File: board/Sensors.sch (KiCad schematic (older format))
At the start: 7 parts, among them Q1 Phototrans, Q2 Q_NPN_BEC, U1 74HC393

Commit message: Updated some refs.
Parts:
- C1: value 0.1uF/25V -> 0.1uF/50V
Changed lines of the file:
@@
 P 3800 3700
 F 0 "C1" H 3915 3746 50  0000 L CNN
-F 1 "0.1uF/25V" H 3915 3655 50  0000 L CNN
+F 1 "0.1uF/50V" H 3915 3655 50  0000 L CNN
 F 2 "Capacitor_SMD:C_0603_1608Metric_Pad1.05x0.95mm_HandSolder" H 3838 3550 50  0001 C CNN
 F 3 "~" H 3800 3700 50  0001 C CNN

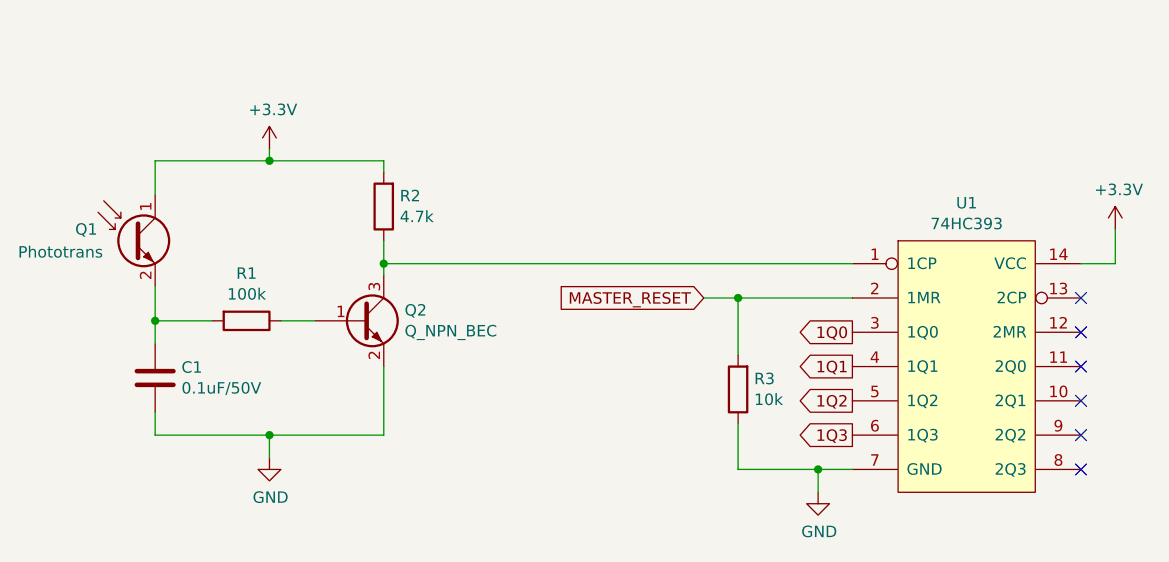
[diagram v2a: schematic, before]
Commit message: Reworked input circuit.
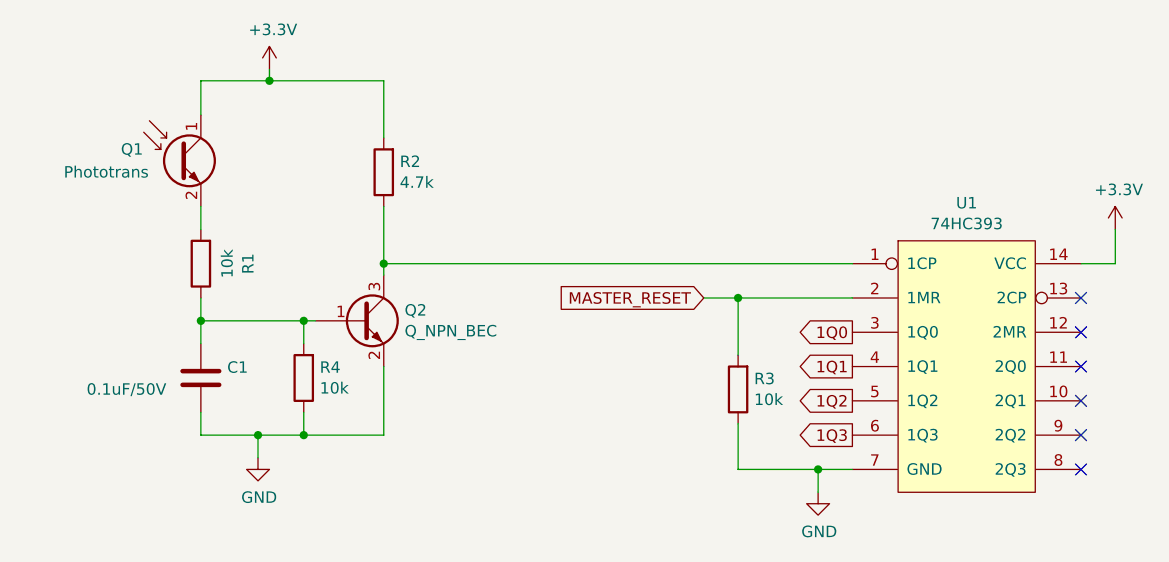
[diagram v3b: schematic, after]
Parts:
- added R4: 10k, Resistor_SMD:R_0603_1608Metric_Pad1.05x0.95mm_HandSolder, symbol Device:R
- R1: value 100k -> 10k
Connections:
- net GND: now also R4.1
- net at Q2.1 (B), R1.1: now also C1.1, R4.2
- net at Q1.2 (E), R1.2: no longer C1.1
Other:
- moved on the sheet: C1, Q1, R1, R2
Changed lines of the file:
@@
 L power:GND #PWR09
 U 1 1 5BE94315
-P 4300 4050
-F 0 "#PWR09" H 4300 3800 50  0001 C CNN
-F 1 "GND" H 4305 3877 50  0000 C CNN
-F 2 "" H 4300 4050 50  0001 C CNN
-F 3 "" H 4300 4050 50  0001 C CNN
-	1    4300 4050
+P 4250 4050
+F 0 "#PWR09" H 4250 3800 50  0001 C CNN
+F 1 "GND" H 4255 3877 50  0000 C CNN
+F 2 "" H 4250 4050 50  0001 C CNN
+F 3 "" H 4250 4050 50  0001 C CNN
+	1    4250 4050
 	1    0    0    -1
 $EndComp
@@
 L Device:C C1
 U 1 1 5BE943F3
-P 3800 3700
-F 0 "C1" H 3915 3746 50  0000 L CNN
-F 1 "0.1uF/50V" H 3915 3655 50  0000 L CNN
-F 2 "Capacitor_SMD:C_0603_1608Metric_Pad1.05x0.95mm_HandSolder" H 3838 3550 50  0001 C CNN
-F 3 "~" H 3800 3700 50  0001 C CNN
-	1    3800 3700
+P 4000 3700
+F 0 "C1" H 4115 3746 50  0000 L CNN
+F 1 "0.1uF/50V" H 3500 3650 50  0000 L CNN
+F 2 "Capacitor_SMD:C_0603_1608Metric_Pad1.05x0.95mm_HandSolder" H 4038 3550 50  0001 C CNN
+F 3 "~" H 4000 3700 50  0001 C CNN
+	1    4000 3700
 	1    0    0    -1
 $EndComp
@@
 L Device:R R1
 U 1 1 5BE944CC
-P 4200 3450
-F 0 "R1" V 3993 3450 50  0000 C CNN
-F 1 "100k" V 4084 3450 50  0000 C CNN
-F 2 "Resistor_SMD:R_0603_1608Metric_Pad1.05x0.95mm_HandSolder" V 4130 3450 50  0001 C CNN
-F 3 "~" H 4200 3450 50  0001 C CNN
-	1    4200 3450
-	0    1    1    0
+P 4000 3200
+F 0 "R1" V 3793 3200 50  0000 C CNN
+F 1 "10k" V 3884 3200 50  0000 C CNN
+F 2 "Resistor_SMD:R_0603_1608Metric_Pad1.05x0.95mm_HandSolder" V 3930 3200 50  0001 C CNN
+F 3 "~" H 4000 3200 50  0001 C CNN
+	1    4000 3200
+	-1   0    0    1
 $EndComp
 $Comp
 L Device:R R2
 U 1 1 5BE94578
-P 4800 2950
-F 0 "R2" H 4730 2904 50  0000 R CNN
-F 1 "4.7k" H 4730 2995 50  0000 R CNN
-F 2 "Resistor_SMD:R_0603_1608Metric_Pad1.05x0.95mm_HandSolder" V 4730 2950 50  0001 C CNN
-F 3 "~" H 4800 2950 50  0001 C CNN
-	1    4800 2950
-	-1   0    0    1
-$EndComp
-Wire Wire Line
-	4800 2800 4800 2750
+P 4800 2800
+F 0 "R2" H 4730 2754 50  0000 R CNN
+F 1 "4.7k" H 4730 2845 50  0000 R CNN
+F 2 "Resistor_SMD:R_0603_1608Metric_Pad1.05x0.95mm_HandSolder" V 4730 2800 50  0001 C CNN
+F 3 "~" H 4800 2800 50  0001 C CNN
+	1    4800 2800
+	-1   0    0    1
+$EndComp
+Wire Wire Line
+	4800 2650 4800 2400
 $Comp
 L power:+3.3V #PWR08
 U 1 1 5BE94675
-P 4300 2700
-F 0 "#PWR08" H 4300 2550 50  0001 C CNN
-F 1 "+3.3V" H 4315 2873 50  0000 C CNN
-F 2 "" H 4300 2700 50  0001 C CNN
-F 3 "" H 4300 2700 50  0001 C CNN
-	1    4300 2700
+P 4300 2350
+F 0 "#PWR08" H 4300 2200 50  0001 C CNN
+F 1 "+3.3V" H 4315 2523 50  0000 C CNN
+F 2 "" H 4300 2350 50  0001 C CNN
+F 3 "" H 4300 2350 50  0001 C CNN
+	1    4300 2350
 	1    0    0    -1
 $EndComp
@@
 	4800 3650 4800 3950
 Wire Wire Line
-	4050 3450 3800 3450
-Wire Wire Line
-	3800 3450 3800 3550
-Wire Wire Line
-	3800 3850 3800 3950
-Wire Wire Line
-	3800 3950 4300 3950
-Wire Wire Line
-	4350 3450 4500 3450
-Wire Wire Line
-	3800 2750 4300 2750
-Wire Wire Line
-	4300 4050 4300 3950
-Connection ~ 4300 3950
-Wire Wire Line
-	4300 3950 4800 3950
-Wire Wire Line
-	4300 2700 4300 2750
-Connection ~ 4300 2750
-Wire Wire Line
-	4300 2750 4800 2750
+	4250 3950 4450 3950
 $Comp
 L Device:Q_Photo_NPN Q1
 U 1 1 5BE97372
-P 3700 3100
-F 0 "Q1" H 3450 3150 50  0000 L CNN
-F 1 "Phototrans" H 3200 3050 50  0000 L CNN
-F 2 "w_conn_mpt:mpt_0,5-2-2,54" H 3900 3200 50  0001 C CNN
-F 3 "~" H 3700 3100 50  0001 C CNN
-F 4 "1497675" H 3700 3100 50  0001 C CNN "Farnell"
-F 5 "TEPT4400" H 3700 3100 50  0001 C CNN "Ref"
-	1    3700 3100
-	1    0    0    -1
-$EndComp
-Wire Wire Line
-	3800 2750 3800 2900
-Wire Wire Line
-	3800 3300 3800 3450
-Connection ~ 3800 3450
-Wire Wire Line
-	4800 3100 4800 3200
+P 3900 2750
+F 0 "Q1" H 3650 2800 50  0000 L CNN
+F 1 "Phototrans" H 3400 2700 50  0000 L CNN
+F 2 "w_conn_mpt:mpt_0,5-2-2,54" H 4100 2850 50  0001 C CNN
+F 3 "~" H 3900 2750 50  0001 C CNN
+F 4 "1497675" H 3900 2750 50  0001 C CNN "Farnell"
+F 5 "TEPT4400" H 3900 2750 50  0001 C CNN "Ref"
+	1    3900 2750
+	1    0    0    -1
+$EndComp
+Wire Wire Line
+	4000 2400 4000 2550
+Wire Wire Line
+	4800 2950 4800 3200
 Wire Wire Line
 	4800 3200 6850 3200
-Connection ~ 4800 3200
 Wire Wire Line
 	4800 3200 4800 3250
@@
 	6350 3350 6850 3350
 Connection ~ 6350 3350
+$Comp
+L Device:R R4
+U 1 1 5D192C7B
+P 4450 3700
+F 0 "R4" H 4380 3654 50  0000 R CNN
+F 1 "10k" H 4380 3745 50  0000 R CNN
+F 2 "Resistor_SMD:R_0603_1608Metric_Pad1.05x0.95mm_HandSolder" V 4380 3700 50  0001 C CNN
+F 3 "~" H 4450 3700 50  0001 C CNN
+	1    4450 3700
+	-1   0    0    1
+$EndComp
+Wire Wire Line
+	4250 3950 4250 4050
+Connection ~ 4250 3950
+Wire Wire Line
+	4450 3450 4450 3550
+Wire Wire Line
+	4450 3850 4450 3950
+Wire Wire Line
+	4300 2400 4800 2400
+Wire Wire Line
+	4300 2350 4300 2400
+Connection ~ 4300 2400
+Wire Wire Line
+	4450 3450 4500 3450
+Connection ~ 4450 3950
+Wire Wire Line
+	4450 3950 4800 3950
+Wire Wire Line
+	4000 3950 4250 3950
+Wire Wire Line
+	4000 2400 4300 2400
+Wire Wire Line
+	4000 2950 4000 3050
+Wire Wire Line
+	4000 3350 4000 3450
+Wire Wire Line
+	4000 3950 4000 3850
+Wire Wire Line
+	4450 3450 4000 3450
+Connection ~ 4450 3450
+Connection ~ 4000 3450
+Wire Wire Line
+	4000 3450 4000 3550
+Connection ~ 4800 3200
 $EndSCHEMATC
